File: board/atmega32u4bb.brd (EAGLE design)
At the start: 30.4 x 12.2 mm, 18 parts, among them X3 16MHz

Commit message: V1 board design
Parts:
- removed BOOT: EVQQ2, adaprog:EVQ-Q2
- removed ISP6: PINHD-2X3, adaprog:2X3SMT
- removed L1: 500mA, adafruit:R1206
- removed R4: 10K, adafruit:R0805
- removed SJ1: HWB, jumper:SJ
- removed U$5: USB_PADS, glowboard:PAD_CONNECTION
- removed X3: 16MHz, adaprog:NX5032
- added Q1: 16 MHz, glowboard:ABMM2_CRYSTAL
- added S1: Normally open, glowboard:KMR211G_SWITCH
- added U$2: MINI_USB, glowboard:MINI_USB_PADS
- added U$4: ICSP, glowboard:ICSP_PADS
- moved C2 5.61 mm to (27.5, 1.86)
- moved C3 5.61 mm to (27.5, 5.14)
- moved C6 5.11 mm to (23.2, 11.1), turned to 0 degrees
- moved R1 4.30 mm to (10.9, 8.01)
- moved R2 4.30 mm to (10.9, 6.25)
- moved C7 4.30 mm to (15.8, 1.06)
- moved C4 4.22 mm to (10.7, 2.97)
- moved U$1 4.20 mm to (17.8, 6.20)
- moved C5 3.91 mm to (10.9, 1.40)
- moved C1 3.10 mm to (14.7, 11.2)
- moved U$3 2.30 mm to (30.8, 6.02)
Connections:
- removed net AREF: U$1.42
- removed net HWB: R4.1, SJ1.1, U$1.33
- removed net N$1: L1.1, U$5.1
- net GND: now also S1.P$1, S1.P$2, U$1.33, U$2.P$5, U$2.P$6, U$2.P$7, U$2.P$8, U$2.P$9, U$4.GND; no longer BOOT.B, BOOT.B', ISP6.6, SJ1.2, U$5.4
- net MISO: now also U$4.MISO; no longer ISP6.1
- net MOSI: now also U$4.MOSI; no longer ISP6.4
- net N$2: now also U$2.P$3; no longer U$5.3
- net N$5: now also U$2.P$2; no longer U$5.2
- net N$8: now also Q1.P$3; no longer X3.P$2
- net N$9: now also Q1.P$1; no longer X3.P$1
- net RST: now also S1.P$3, S1.P$4, U$4.RST; no longer BOOT.A, BOOT.A', ISP6.5
- net SCK: now also U$4.SCK`; no longer ISP6.3
- net VCC: now also U$1.42, U$2.P$1, U$4.VCC; no longer ISP6.2, L1.2, R4.2
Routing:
- net GND: track 50.1 -> 96.0 mm, vias 2 -> 3
- net VCC: track 38.5 -> 71.5 mm, vias 5 -> 7
- net N$9: track 0.00 -> 15.0 mm
- net RST: track 17.5 -> 24.1 mm, vias 1 -> 3
- net SCK: track 21.3 -> 27.9 mm
- net N$8: track 7.18 -> 12.6 mm
- net N$1: track 3.47 -> 0.00 mm
- net MOSI: track 23.7 -> 26.4 mm
- net N$2: track 4.89 -> 2.87 mm
- net N$5: track 4.36 -> 3.30 mm
- net MISO: track 19.0 -> 18.0 mm
- net +3V3: track 6.84 -> 6.00 mm
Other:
- board size 30.4 x 12.2 mm -> 33 x 12.2 mm

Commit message: Fix some errors
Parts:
- removed C5: 10uF, adafruit:A/3216-18R
- added C8: 0.1uF, adafruit:C0805K
- added U$5: EXPANSION_HEADER, glowboard:EXPANSION_HEADER
- moved C4 8.10 mm to (10.7, 11.1)
- moved C1 0.70 mm to (14.0, 11.2)
- moved R1 0.45 mm to (10.7, 7.61)
- moved R2 0.36 mm to (10.7, 5.95)
- moved Q1 0.10 mm to (24.6, 3.50)
- moved C3 0.10 mm to (27.5, 5.24)
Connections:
- new net N$1: U$1.41, U$5.P$1
- new net N$6: U$1.37, U$5.P$2
- new net N$7: U$1.36, U$5.P$3
- net GND: now also C8.2; no longer C5.-
- net VCC: now also C8.1; no longer C5.+
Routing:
- net N$7: track 0.00 -> 2.17 mm
- net N$1: track 0.00 -> 2.06 mm
- net VCC: track 71.5 -> 69.6 mm
- net N$6: track 0.00 -> 1.77 mm
- net MOSI: track 26.4 -> 25.2 mm
- net SCK: track 27.9 -> 26.8 mm
- net N$3: track 2.76 -> 3.59 mm
- net N$9: track 15.0 -> 14.2 mm
- net N$4: track 3.34 -> 4.12 mm

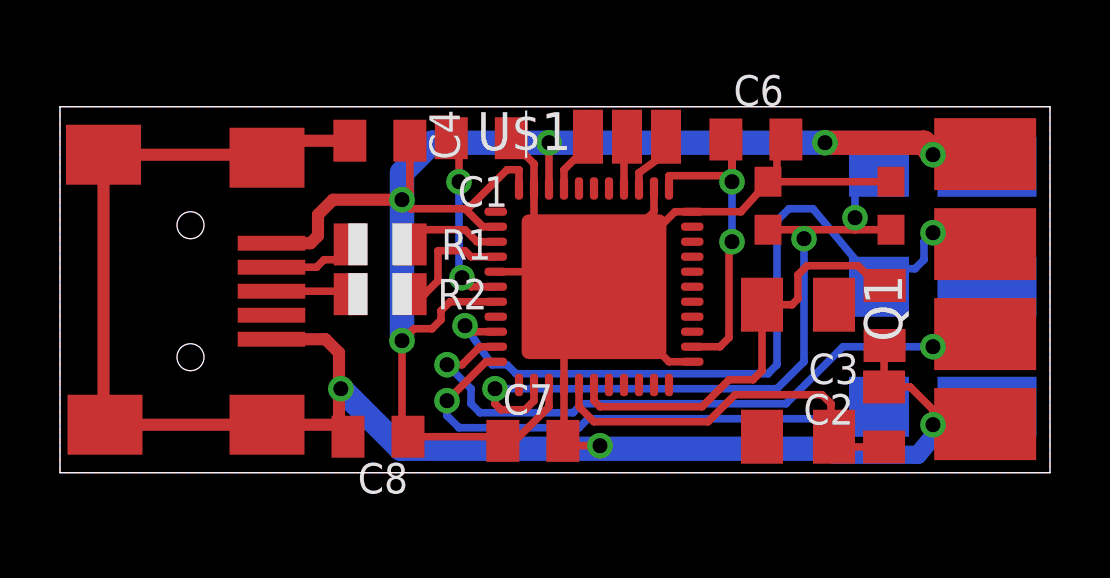
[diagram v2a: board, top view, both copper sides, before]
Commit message: Passes DRC, add expansion header, move switch to non-reset pin.
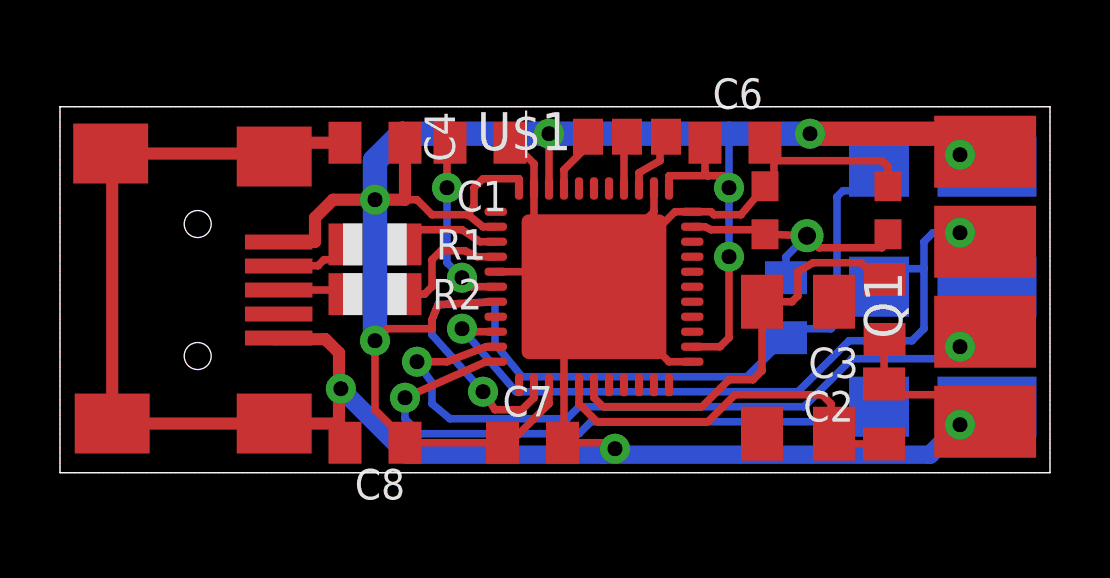
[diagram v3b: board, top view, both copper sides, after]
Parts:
- removed U$2: MINI_USB, glowboard:MINI_USB_PADS
- added C5: 0uF (DNC), adafruit:C0805K
- added U$6: GLOWBOARD_MINI_USB, blinkyboard:GLOWBOARD_MINI_USB_PADS
- U$5: value EXPANSION_HEADER -> GLOWBOARD_EXPANSION_HEADER; device glowboard:EXPANSION_HEADER -> blinkyboard:GLOWBOARD_EXPANSION_HEADER
- moved C6 0.70 mm to (22.5, 11.0)
- moved C8 0.22 mm to (10.5, 1.00)
- moved C3 0.20 mm to (27.5, 5.44)
- moved S1 0.18 mm to (25.5, 8.75)
- moved C4 0.17 mm to (10.5, 11.0)
- moved R1 0.17 mm to (10.5, 7.61)
- moved R2 0.17 mm to (10.5, 5.95)
- moved C1 0.16 mm to (14.0, 11.0)
- moved C2 0.10 mm to (27.5, 1.96)
- moved Q1 0.10 mm to (24.6, 3.60)
- moved U$3 0.08 mm to (30.8, 6.10)
- moved C7 0.06 mm to (15.8, 1.00)
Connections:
- new net N$10: C5.2, S1.P$3, S1.P$4, U$1.32
- net GND: now also U$6.P$5, U$6.P$6, U$6.P$7, U$6.P$8, U$6.P$9; no longer U$2.P$5, U$2.P$6, U$2.P$7, U$2.P$8, U$2.P$9
- net N$2: now also U$6.P$3; no longer U$2.P$3
- net N$5: now also U$6.P$2; no longer U$2.P$2
- net RST: now also C5.1; no longer S1.P$3, S1.P$4
- net VCC: now also U$6.P$1; no longer U$2.P$1
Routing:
- net N$10: track 0.00 -> 8.98 mm, vias 0 -> 1
- net RST: track 24.2 -> 28.2 mm, vias 3 -> 1
- net MISO: track 17.8 -> 20.7 mm
- net GND: track 96.1 -> 98.0 mm
- net MOSI: track 25.2 -> 26.5 mm
- net SCK: track 26.8 -> 26.1 mm
- net VCC: track 69.6 -> 70.1 mm
